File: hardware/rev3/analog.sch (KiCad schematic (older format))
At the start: 21 parts, among them U4 AD9102, X1 LMK61XX

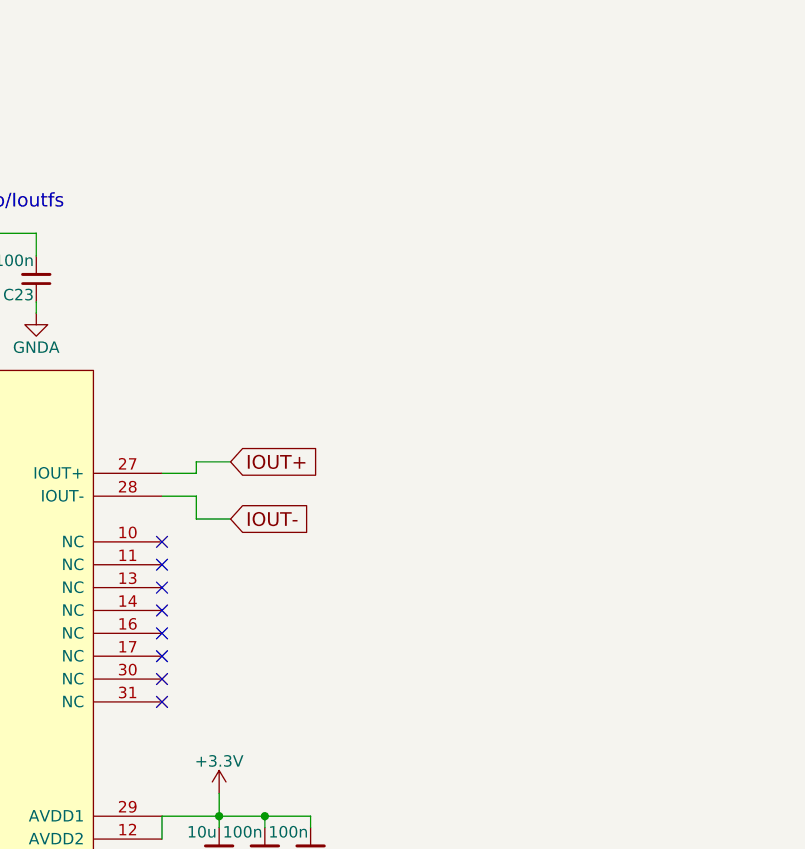
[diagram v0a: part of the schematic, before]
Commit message: Add initial output amplifier design.
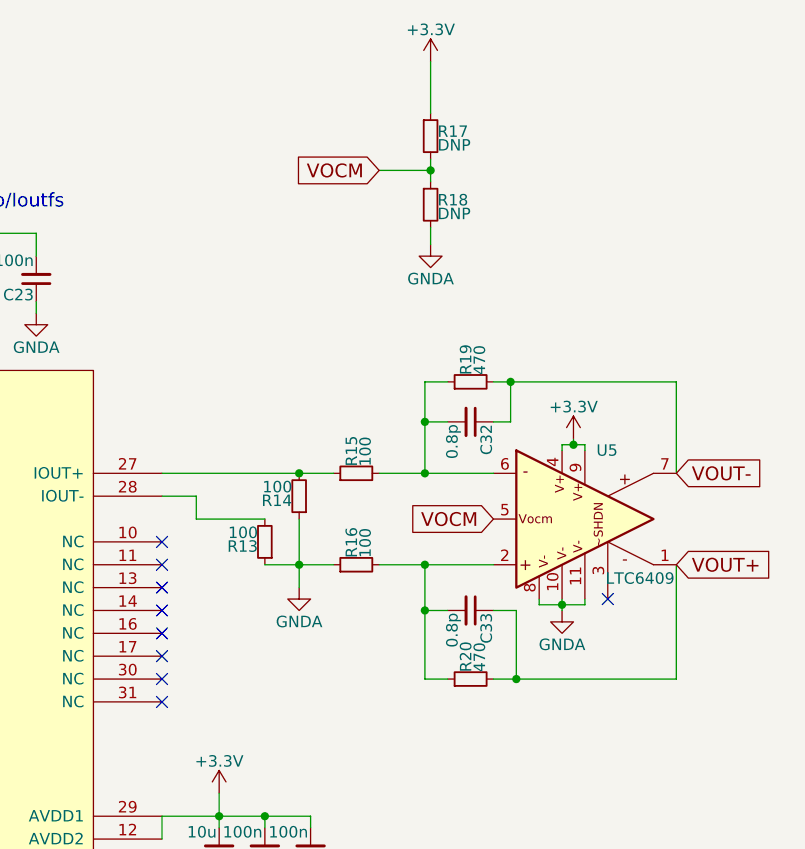
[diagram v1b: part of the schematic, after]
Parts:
- added C32, C33: 0.8p, symbol C_Small
- added R13, R14, R15, R16: 100, symbol R_Small
- added R17, R18: DNP, symbol R_Small
- added R19, R20: 470, symbol R_Small
- added U5: LTC6409, symbol LTC6409
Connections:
- net +3V3: now also R17.1, U5.4, U5.9
- net GNDA: now also R13.1, R14.1, R16.1, R18.2, U5.10, U5.11, U5.8
- net IOUT+: no longer names the net of U4.27 (IOUT+)
- net IOUT+: now also R14.2, R15.1
- net IOUT-: no longer names the net of U4.28 (IOUT-)
- net IOUT-: now also R13.2
- new net: C33.2, R16.2, R20.1, U5.2
- new net: C32.2, R15.2, R19.1, U5.6
- new net VOCM: R17.2, R18.1, U5.5
- new net VOUT+: C33.1, R20.2, U5.1
- new net VOUT-: C32.1, R19.2, U5.7
- no-connect marks 10 -> 11

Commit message: Add bypass caps to output amp.
Fixes #4.
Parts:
- added C? (x2): 100n, symbol C_Small
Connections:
- net +3V3: now also C?.2, C?.2; no longer U5.4, U5.9
- new net: C?.1, C?.1, U5.4, U5.9
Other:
- note added: "Ioutfs=4mA\nVin=Vin+-Vin=Ioutfs*R=400mV\nVout=Rf/Ri*Vin=1.88V"
- moved on the sheet: R13, R14

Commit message: Finish up output amp schematic.
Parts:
- added C22, C29: 10u, symbol C_Small
- added C27, C31: 2.8p, symbol C_Small
- added C28: 100n, symbol C_Small
- added L3, L4: 800m, symbol Ferrite_Bead_Small
- added R14, R23: 1.5k, symbol R_Small
- added R18, R21: 1k, symbol R_Small
- added R25, R29: 4.7k, symbol R_Small
- added R26, R28: 10k, symbol R_Small
- added U5: LTC6269, symbol LTC6269
- R12: renamed from R19; value 470 -> 500
- R27: renamed from R20; value 470 -> 500
- gave numbers to parts that had none: 2
- renumbered C23 to C24, C32 to C26, C27 to C30, C33 to C32, C28 to C33, C24 to C34, C25 to C35, C26 to C36, C18 to C37, C19 to C38, C20 to C39, C21 to C40, C22 to C41, C29 to C42, C30 to C43, C31 to C44, R18 to R10, R10 to R11, R12 to R13, R8 to R16, R9 to R17, R13 to R19, R14 to R20, R16 to R22, R11 to R24, R17 to R9, U5 to U4, U4 to U6
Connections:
- net +3V3: now also C23.1, C25.1, U4.4, U4.9, C22.1, C28.1, C29.1, R26.1, U5.10 (V+); no longer C23.2, C25.2
- net GNDA: now also C23.2, C25.2, C22.2, C28.2, C29.2, R25.2, R28.2, R29.2, U5.11 (V-), U5.4 (V-)
- net VOUT+: now also R21.1
- net VOUT-: now also R18.1
- net at U4.3: now also L4.2, R29.1
- new net: C27.1, R14.2, R18.2, U5.2 (-A)
- new net: C31.2, R21.2, R23.1, U5.3 (+A)
- new net: L3.1, R25.1, U5.5 (~SDA), U5.6 (~SDB)
- new net: R26.2, R28.1, U5.7 (+B)
- new net: C31.1, R23.2, U5.8 (-B), U5.9
- new net AMP0_EN: L4.1
- new net AMP1_EN: L3.2
- new net VOUT: C27.2, R14.1, U5.1
- no-connect marks 11 -> 10
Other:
- note added: "Pin 4"
- note added: "Pin 9"
- note removed: "Ioutfs=4mA\nVin=Vin+-Vin=Ioutfs*R=400mV\nVout=Rf/Ri*Vin=1.88V"
- note removed: "Ioutfs=4mA\nVrefio=1V\nRcal_sense=32*Vrefio/Ioutfs"
- moved on the sheet: C23, C25

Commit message: Add missing footprints.
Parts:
- C22, C23, C24, C25, C26, C27, C28, C29, C30, C31, C32, C33, C34, C35, C36, C37, C38, C39, C40, C41, C42, C43, C44: footprint (none) -> Capacitors_SMD:C_0603_HandSoldering
- L3, L4: footprint (none) -> Inductors_SMD:L_0603_HandSoldering
- R10, R11, R12, R13, R14, R15, R16, R17, R18, R19, R20, R21, R22, R23, R24, R25, R26, R27, R28, R29, R9: footprint (none) -> Resistors_SMD:R_0603_HandSoldering
- U4: footprint (none) -> footprints:LTC6409-UDB
- U5: footprint (none) -> footprints:LTC6269-10DFN
- U6: footprint MODULE -> footprints:AD9102-10LFCSP
- X1: value LMK61XX -> DSC1123; footprint MODULE -> footprints:7050XO; DigiKey 296-43860-1-ND -> 576-4642-ND; Fieldname (none) -> Value

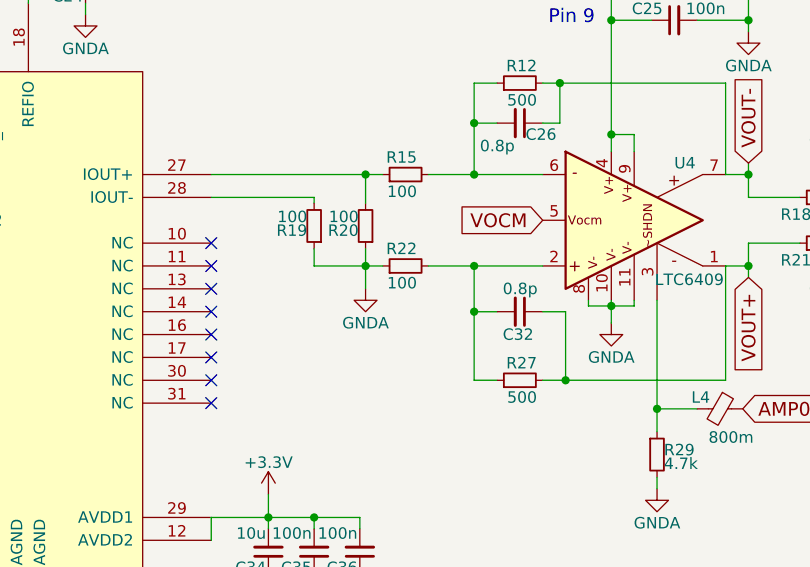
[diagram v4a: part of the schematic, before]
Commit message: Fix incorrect connection to output amp.
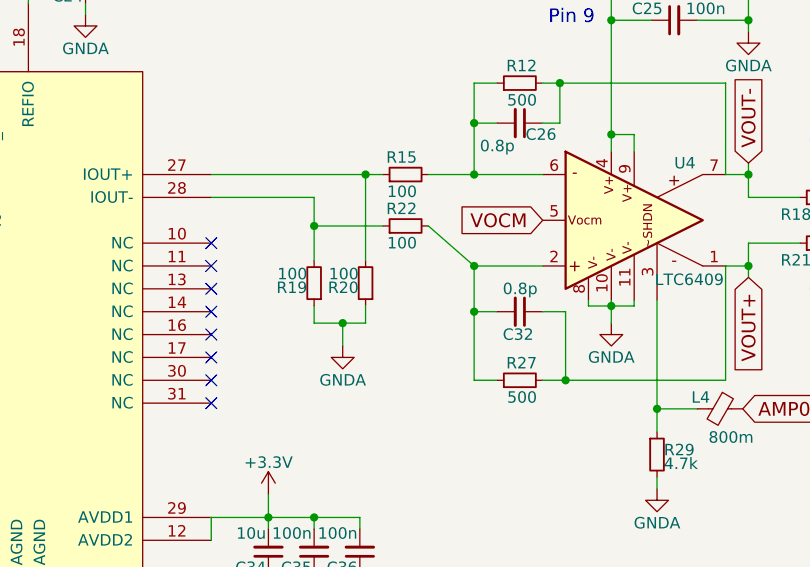
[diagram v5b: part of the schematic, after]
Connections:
- net GNDA: no longer R22.1
- net at R19.2, U6.28 (IOUT-): now also R22.1
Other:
- moved on the sheet: R19, R20, R22
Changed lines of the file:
@@
 L R_Small R19
 U 1 1 58FD676A
-P 6550 3125
-F 0 "R19" H 6580 3145 50  0000 L CNN
-F 1 "100" H 6580 3085 50  0000 L CNN
-F 2 "Resistors_SMD:R_0603_HandSoldering" H 6550 3125 50  0001 C CNN
-F 3 "" H 6550 3125 50  0001 C CNN
-	1    6550 3125
+P 6550 3375
+F 0 "R19" H 6580 3395 50  0000 L CNN
+F 1 "100" H 6580 3335 50  0000 L CNN
+F 2 "Resistors_SMD:R_0603_HandSoldering" H 6550 3375 50  0001 C CNN
+F 3 "" H 6550 3375 50  0001 C CNN
+	1    6550 3375
 	-1   0    0    1
 $EndComp
@@
 L R_Small R20
 U 1 1 58FD6A4A
-P 6775 3125
-F 0 "R20" H 6805 3145 50  0000 L CNN
-F 1 "100" H 6805 3085 50  0000 L CNN
-F 2 "Resistors_SMD:R_0603_HandSoldering" H 6775 3125 50  0001 C CNN
-F 3 "" H 6775 3125 50  0001 C CNN
-	1    6775 3125
+P 6775 3375
+F 0 "R20" H 6805 3395 50  0000 L CNN
+F 1 "100" H 6805 3335 50  0000 L CNN
+F 2 "Resistors_SMD:R_0603_HandSoldering" H 6775 3375 50  0001 C CNN
+F 3 "" H 6775 3375 50  0001 C CNN
+	1    6775 3375
 	-1   0    0    1
 $EndComp
@@
 L GNDA #PWR041
 U 1 1 58FD7350
-P 6775 3400
-F 0 "#PWR041" H 6775 3150 50  0001 C CNN
-F 1 "GNDA" H 6775 3250 50  0000 C CNN
-F 2 "" H 6775 3400 50  0001 C CNN
-F 3 "" H 6775 3400 50  0001 C CNN
-	1    6775 3400
+P 6675 3650
+F 0 "#PWR041" H 6675 3400 50  0001 C CNN
+F 1 "GNDA" H 6675 3500 50  0000 C CNN
+F 2 "" H 6675 3650 50  0001 C CNN
+F 3 "" H 6675 3650 50  0001 C CNN
+	1    6675 3650
 	1    0    0    -1
 $EndComp
@@
 L R_Small R22
 U 1 1 58FD8D9B
-P 6950 3300
-F 0 "R22" V 7025 3250 50  0000 L CNN
-F 1 "100" V 6875 3250 50  0000 L CNN
-F 2 "Resistors_SMD:R_0603_HandSoldering" H 6950 3300 50  0001 C CNN
-F 3 "" H 6950 3300 50  0001 C CNN
-	1    6950 3300
+P 6950 3125
+F 0 "R22" V 7025 3075 50  0000 L CNN
+F 1 "100" V 6875 3075 50  0000 L CNN
+F 2 "Resistors_SMD:R_0603_HandSoldering" H 6950 3125 50  0001 C CNN
+F 3 "" H 6950 3125 50  0001 C CNN
+	1    6950 3125
 	0    -1   -1   0
 $EndComp
@@
 	3550 2600 3550 2550
 Wire Wire Line
-	6775 3225 6775 3400
-Wire Wire Line
-	6550 3300 6850 3300
-Connection ~ 6775 3300
+	6675 3550 6675 3650
+Connection ~ 6675 3550
 Connection ~ 6775 2900
 Wire Wire Line
@@
 Connection ~ 7250 2900
 Wire Wire Line
-	7050 3300 7550 3300
+	7050 3125 7250 3300
+Wire Wire Line
+	7250 3300 7550 3300
 Wire Wire Line
 	7550 2500 8350 2500
@@
 $EndComp
 Wire Wire Line
-	6550 3000 6550 3025
-Wire Wire Line
-	6550 3300 6550 3225
-Wire Wire Line
-	6775 3025 6775 2900
+	6550 3000 6550 3275
+Wire Wire Line
+	6550 3550 6550 3475
+Wire Wire Line
+	6775 2900 6775 3275
 $Comp
 L R_Small R29
@@
 	8450 1700 8225 1700
 Connection ~ 8450 1950
+Wire Wire Line
+	6550 3550 6775 3550
+Wire Wire Line
+	6775 3550 6775 3475
+Wire Wire Line
+	6850 3125 6550 3125
+Connection ~ 6550 3125
 $EndSCHEMATC

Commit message: Add decoupling to biasing amp.
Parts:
- added C45: 4.7u, Capacitors_SMD:C_0603_HandSoldering, symbol C_Small
- added C46: 1u, Capacitors_SMD:C_0603_HandSoldering, symbol C_Small
- added R30: 50k, Resistors_SMD:R_0603_HandSoldering, symbol R_Small
- R26, R28: value 10k -> 100k
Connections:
- net GNDA: now also C45.2, C46.2
- net at R26.2, R28.1, U5.7 (+B): now also C46.1
- net at C31.1, R23.2, U5.9: now also C45.1, R30.2; no longer U5.8 (-B)
- new net: R30.1, U5.8 (-B)
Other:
- moved on the sheet: R26, R28
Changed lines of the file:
@@
 	8950 3525 9125 3525
 Wire Wire Line
-	9125 3525 9125 4275
+	9125 3525 9125 4400
 Wire Wire Line
 	9125 3750 9350 3750
@@
 L R_Small R26
 U 1 1 590277EA
-P 10500 3650
-F 0 "R26" V 10425 3600 50  0000 L CNN
-F 1 "10k" V 10575 3600 50  0000 L CNN
-F 2 "Resistors_SMD:R_0603_HandSoldering" H 10500 3650 50  0001 C CNN
-F 3 "" H 10500 3650 50  0001 C CNN
-	1    10500 3650
+P 10700 3650
+F 0 "R26" V 10625 3600 50  0000 L CNN
+F 1 "100k" V 10775 3600 50  0000 L CNN
+F 2 "Resistors_SMD:R_0603_HandSoldering" H 10700 3650 50  0001 C CNN
+F 3 "" H 10700 3650 50  0001 C CNN
+	1    10700 3650
 	0    1    1    0
 $EndComp
@@
 L R_Small R28
 U 1 1 590279CA
-P 10275 3800
-F 0 "R28" H 10305 3820 50  0000 L CNN
-F 1 "10k" H 10305 3760 50  0000 L CNN
-F 2 "Resistors_SMD:R_0603_HandSoldering" H 10275 3800 50  0001 C CNN
-F 3 "" H 10275 3800 50  0001 C CNN
-	1    10275 3800
-	1    0    0    -1
-$EndComp
-Wire Wire Line
-	9950 3650 10400 3650
-Connection ~ 10275 3650
+P 10250 3800
+F 0 "R28" H 10280 3820 50  0000 L CNN
+F 1 "100k" H 10280 3760 50  0000 L CNN
+F 2 "Resistors_SMD:R_0603_HandSoldering" H 10250 3800 50  0001 C CNN
+F 3 "" H 10250 3800 50  0001 C CNN
+	1    10250 3800
+	1    0    0    -1
+$EndComp
+Wire Wire Line
+	9950 3650 10600 3650
+Connection ~ 10250 3650
 $Comp
 L GNDA #PWR047
 U 1 1 59027DEB
-P 10275 4000
-F 0 "#PWR047" H 10275 3750 50  0001 C CNN
-F 1 "GNDA" H 10275 3850 50  0000 C CNN
-F 2 "" H 10275 4000 50  0001 C CNN
-F 3 "" H 10275 4000 50  0001 C CNN
-	1    10275 4000
-	1    0    0    -1
-$EndComp
-Wire Wire Line
-	10275 3900 10275 4000
+P 10250 4000
+F 0 "#PWR047" H 10250 3750 50  0001 C CNN
+F 1 "GNDA" H 10250 3850 50  0000 C CNN
+F 2 "" H 10250 4000 50  0001 C CNN
+F 3 "" H 10250 4000 50  0001 C CNN
+	1    10250 4000
+	1    0    0    -1
+$EndComp
+Wire Wire Line
+	10250 3900 10250 4000
 $Comp
 L +3.3V #PWR048
 U 1 1 59027F6D
-P 10675 3575
-F 0 "#PWR048" H 10675 3425 50  0001 C CNN
-F 1 "+3.3V" H 10675 3715 50  0000 C CNN
-F 2 "" H 10675 3575 50  0001 C CNN
-F 3 "" H 10675 3575 50  0001 C CNN
-	1    10675 3575
-	1    0    0    -1
-$EndComp
-Wire Wire Line
-	10600 3650 10675 3650
-Wire Wire Line
-	10675 3650 10675 3575
-Wire Wire Line
-	10275 3650 10275 3700
-Wire Wire Line
-	9950 3850 9950 4275
-Wire Wire Line
-	9950 4275 9125 4275
+P 10800 3575
+F 0 "#PWR048" H 10800 3425 50  0001 C CNN
+F 1 "+3.3V" H 10800 3715 50  0000 C CNN
+F 2 "" H 10800 3575 50  0001 C CNN
+F 3 "" H 10800 3575 50  0001 C CNN
+	1    10800 3575
+	1    0    0    -1
+$EndComp
+Wire Wire Line
+	10250 3650 10250 3700
+Wire Wire Line
+	9950 3850 9950 4400
 Connection ~ 9125 3750
 Wire Wire Line
@@
 	10100 3600 10100 3950
 Wire Wire Line
-	10100 3950 10275 3950
-Connection ~ 10275 3950
+	10100 3950 10525 3950
+Connection ~ 10250 3950
 Text GLabel 10125 2425 2    60   Input ~ 0
 VOUT
@@
 	6850 3125 6550 3125
 Connection ~ 6550 3125
+$Comp
+L C_Small C46
+U 1 1 59041C2E
+P 10525 3800
+F 0 "C46" H 10535 3870 50  0000 L CNN
+F 1 "1u" H 10535 3720 50  0000 L CNN
+F 2 "Capacitors_SMD:C_0603_HandSoldering" H 10525 3800 50  0001 C CNN
+F 3 "" H 10525 3800 50  0001 C CNN
+	1    10525 3800
+	1    0    0    -1
+$EndComp
+Wire Wire Line
+	10525 3700 10525 3650
+Connection ~ 10525 3650
+Wire Wire Line
+	10525 3950 10525 3900
+Wire Wire Line
+	10800 3650 10800 3575
+$Comp
+L R_Small R30
+U 1 1 59042814
+P 9550 4400
+F 0 "R30" V 9475 4350 50  0000 L CNN
+F 1 "50k" V 9625 4350 50  0000 L CNN
+F 2 "Resistors_SMD:R_0603_HandSoldering" H 9550 4400 50  0001 C CNN
+F 3 "" H 9550 4400 50  0001 C CNN
+	1    9550 4400
+	0    1    1    0
+$EndComp
+Wire Wire Line
+	9125 4400 9450 4400
+Wire Wire Line
+	9950 4400 9650 4400
+$Comp
+L C_Small C45
+U 1 1 590448EE
+P 8900 4300
+F 0 "C45" H 8910 4370 50  0000 L CNN
+F 1 "4.7u" H 8910 4220 50  0000 L CNN
+F 2 "Capacitors_SMD:C_0603_HandSoldering" H 8900 4300 50  0001 C CNN
+F 3 "" H 8900 4300 50  0001 C CNN
+	1    8900 4300
+	1    0    0    -1
+$EndComp
+Wire Wire Line
+	8900 4200 8900 4100
+Wire Wire Line
+	8900 4100 9125 4100
+Connection ~ 9125 4100
+$Comp
+L GNDA #PWR053
+U 1 1 59045148
+P 8900 4400
+F 0 "#PWR053" H 8900 4150 50  0001 C CNN
+F 1 "GNDA" H 8900 4250 50  0000 C CNN
+F 2 "" H 8900 4400 50  0001 C CNN
+F 3 "" H 8900 4400 50  0001 C CNN
+	1    8900 4400
+	1    0    0    -1
+$EndComp
 $EndSCHEMATC

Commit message: First routing attempt.
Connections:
- net +1.65V: now reaches C31.1, C45.1, R23.2, R30.2, U5.9
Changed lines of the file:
@@
 	1    0    0    -1
 $EndComp
+Text Label 9125 3755 3    60   ~ 0
++1.65V
 $EndSCHEMATC

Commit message: Update component selection based on digikey availability.
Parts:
- R11: value 8k -> 8.25k
- R12, R27: value 500 -> 510
- R26, R28: value 100k -> 36k
- R30: value 50k -> 18k
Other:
- note added: "Ioutfs=4.034mA\nVoutfs=403.4mV\nVout_diff=5.1*Voutfs=2.057V\nVout=1.5*Vout_diff=3.086V"
- note added: "Target Ioutfs=4mA\nVrefio=1.04 V (nominal)\nIref=Vrefio/Rset=126uA\nIoutfs=32*Iref=4.034mA"
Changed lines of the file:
@@
 P 4800 2000
 F 0 "R11" H 4830 2020 50  0000 L CNN
-F 1 "8k" H 4830 1960 50  0000 L CNN
+F 1 "8.25k" H 4830 1960 50  0000 L CNN
 F 2 "Resistors_SMD:R_0603_HandSoldering" H 4800 2000 50  0001 C CNN
 F 3 "" H 4800 2000 50  0001 C CNN
@@
 P 7450 2500
 F 0 "R12" V 7525 2425 50  0000 L CNN
-F 1 "500" V 7375 2425 50  0000 L CNN
+F 1 "510" V 7375 2425 50  0000 L CNN
 F 2 "Resistors_SMD:R_0603_HandSoldering" H 7450 2500 50  0001 C CNN
 F 3 "" H 7450 2500 50  0001 C CNN
@@
 P 7450 3800
 F 0 "R27" V 7525 3725 50  0000 L CNN
-F 1 "500" V 7375 3725 50  0000 L CNN
+F 1 "510" V 7375 3725 50  0000 L CNN
 F 2 "Resistors_SMD:R_0603_HandSoldering" H 7450 3800 50  0001 C CNN
 F 3 "" H 7450 3800 50  0001 C CNN
@@
 P 10700 3650
 F 0 "R26" V 10625 3600 50  0000 L CNN
-F 1 "100k" V 10775 3600 50  0000 L CNN
+F 1 "36k" V 10775 3600 50  0000 L CNN
 F 2 "Resistors_SMD:R_0603_HandSoldering" H 10700 3650 50  0001 C CNN
 F 3 "" H 10700 3650 50  0001 C CNN
@@
 P 10250 3800
 F 0 "R28" H 10280 3820 50  0000 L CNN
-F 1 "100k" H 10280 3760 50  0000 L CNN
+F 1 "36k" H 10280 3760 50  0000 L CNN
 F 2 "Resistors_SMD:R_0603_HandSoldering" H 10250 3800 50  0001 C CNN
 F 3 "" H 10250 3800 50  0001 C CNN
@@
 P 9550 4400
 F 0 "R30" V 9475 4350 50  0000 L CNN
-F 1 "50k" V 9625 4350 50  0000 L CNN
+F 1 "18k" V 9625 4350 50  0000 L CNN
 F 2 "Resistors_SMD:R_0603_HandSoldering" H 9550 4400 50  0001 C CNN
 F 3 "" H 9550 4400 50  0001 C CNN
@@
 Text Label 9125 3755 3    60   ~ 0
 +1.65V
+Text Notes 4235 1700 0    60   ~ 0
+Target Ioutfs=4mA\nVrefio=1.04 V (nominal)\nIref=Vrefio/Rset=126uA\nIoutfs=32*Iref=4.034mA
+Text Notes 5925 2480 0    60   ~ 0
+Ioutfs=4.034mA\nVoutfs=403.4mV\nVout_diff=5.1*Voutfs=2.057V\nVout=1.5*Vout_diff=3.086V
 $EndSCHEMATC
